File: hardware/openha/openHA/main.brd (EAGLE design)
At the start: 20 x 10 mm, 69 parts, among them IC1 MBN52832, J1 HP_Con, J2 MICRO-USB-RECEPTACLE47589-0001, J3 Bat_Con, U1 STM32L476JX, U2 PCM1774RGPR, U4 STG3693QTR, U5 STBCFG01JR, U6 LD39115J, U7 LD39115J, X1 32.768kHz

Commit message: WIP-BOM Update
Update USB case
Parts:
- added L1: 330Ohms - 600mA, OAlib:C0402
- moved L3 35.5 mm to (15.7, 9.14)
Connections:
- removed net GND: C26.2, C27.2, C41.2, IC1.19, IC1.30, IC1.31, IC1.32, IC1.33, IC1.34, IC1.35, IC1.5
- new net N$12: D3.1, J2.1, L3.2
- new net N$8: J2.CASING1, J2.CASING2, J2.CASING3, J2.CASING4, J2.CASING5, J2.CASING6, J2.CASING7, J2.CASING8, L1.1
- net DGND: now also C26.2, C27.2, C41.2, IC1.19, IC1.30, IC1.31, IC1.32, IC1.33, IC1.34, IC1.35, IC1.5, L1.2; no longer J2.CASING1, J2.CASING2, J2.CASING3, J2.CASING4
- net V_USB: no longer D3.1, J2.1, L3.2

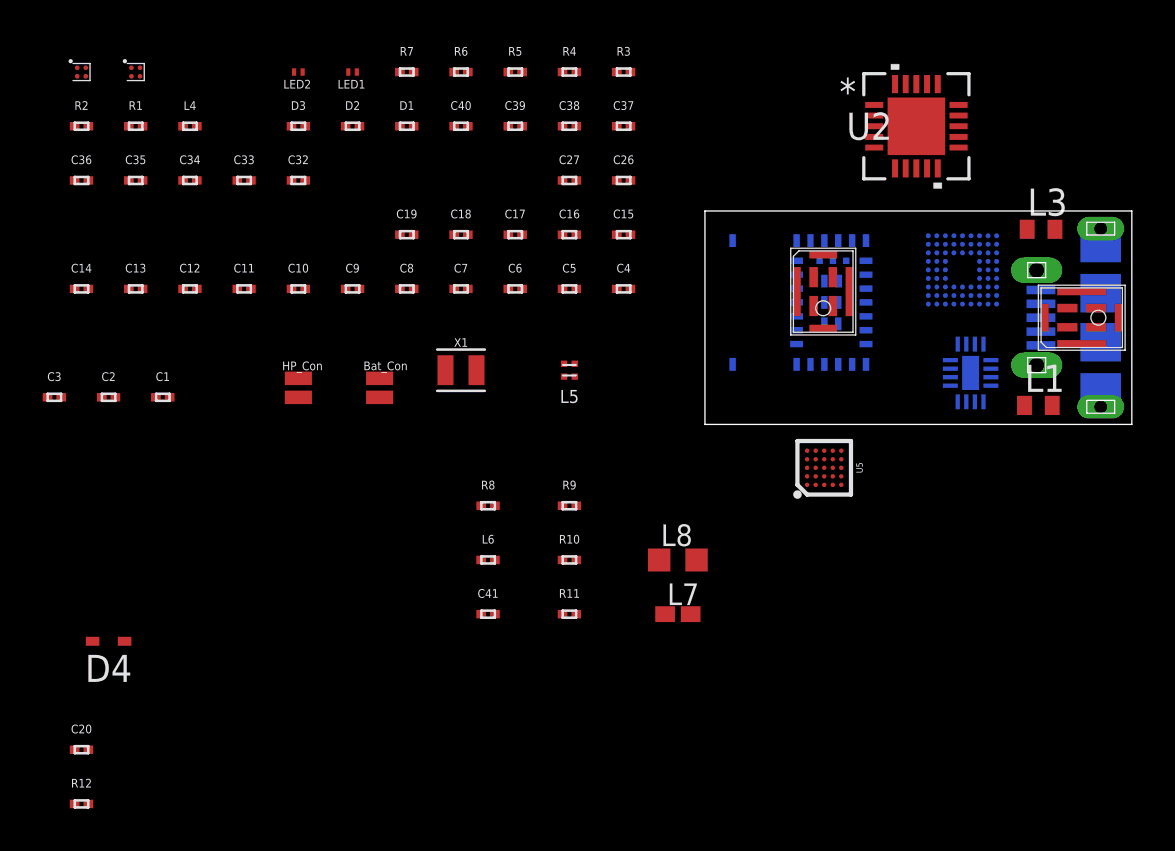
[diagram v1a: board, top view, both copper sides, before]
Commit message: Footprint update
Update some footprint
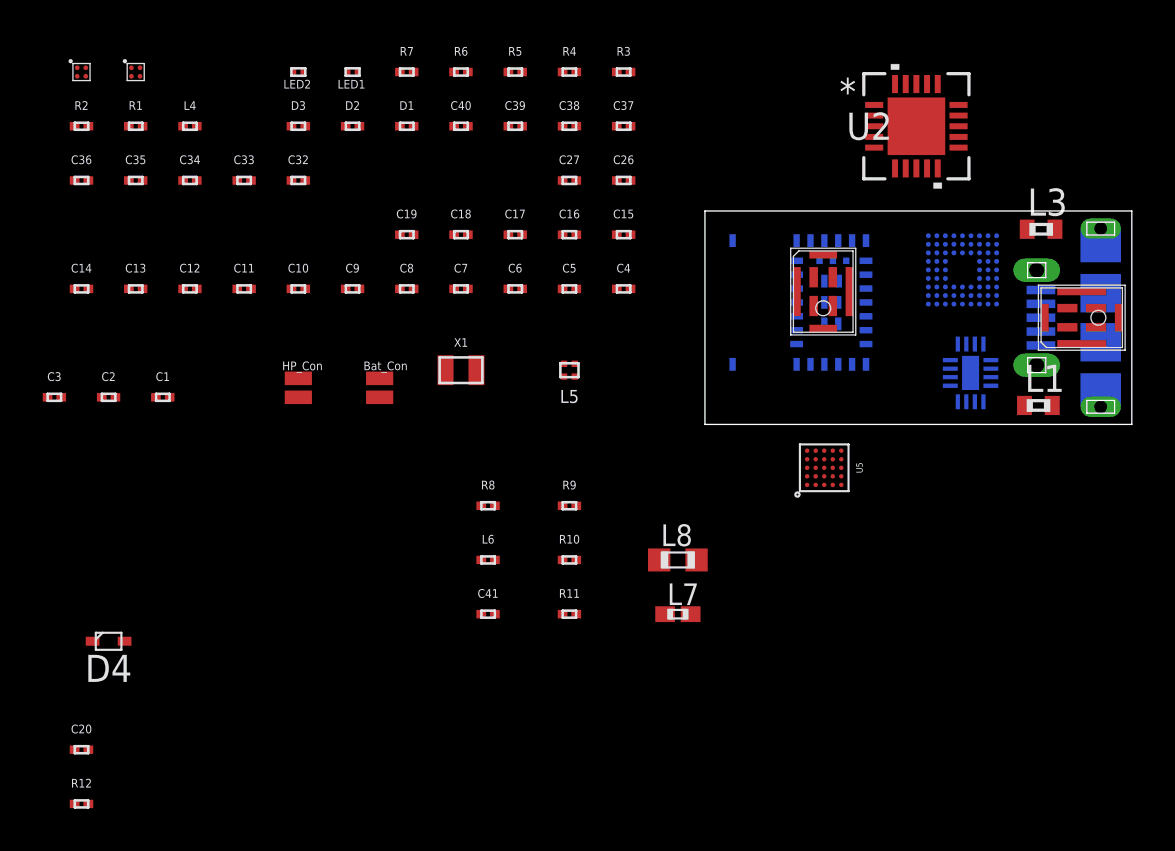
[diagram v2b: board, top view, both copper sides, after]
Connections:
- net SEL_STM_BLU: now also R9.2, U1.J4
- net SEL_SWD_USB: no longer R9.2, U1.J4
